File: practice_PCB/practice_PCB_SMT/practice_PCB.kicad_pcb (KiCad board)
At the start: 2 copper layers, 24.4 x 24.1 mm, 23 parts, among them J1 5V, J2 GND

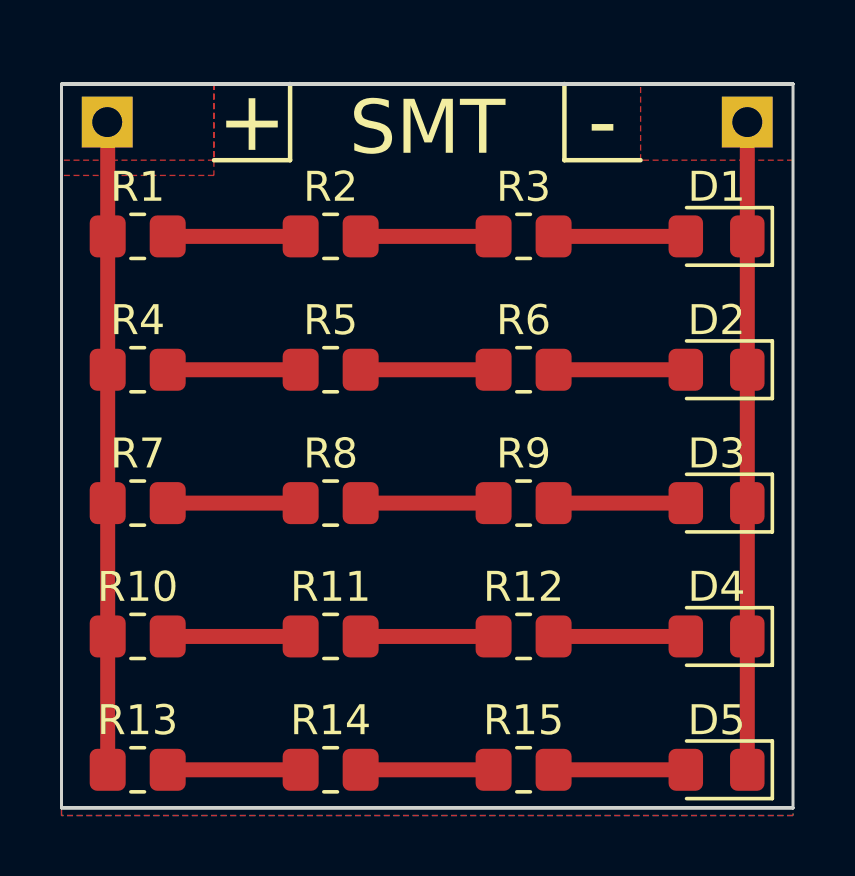
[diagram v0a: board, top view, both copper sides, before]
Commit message: fix some errors with the edge Cut Line
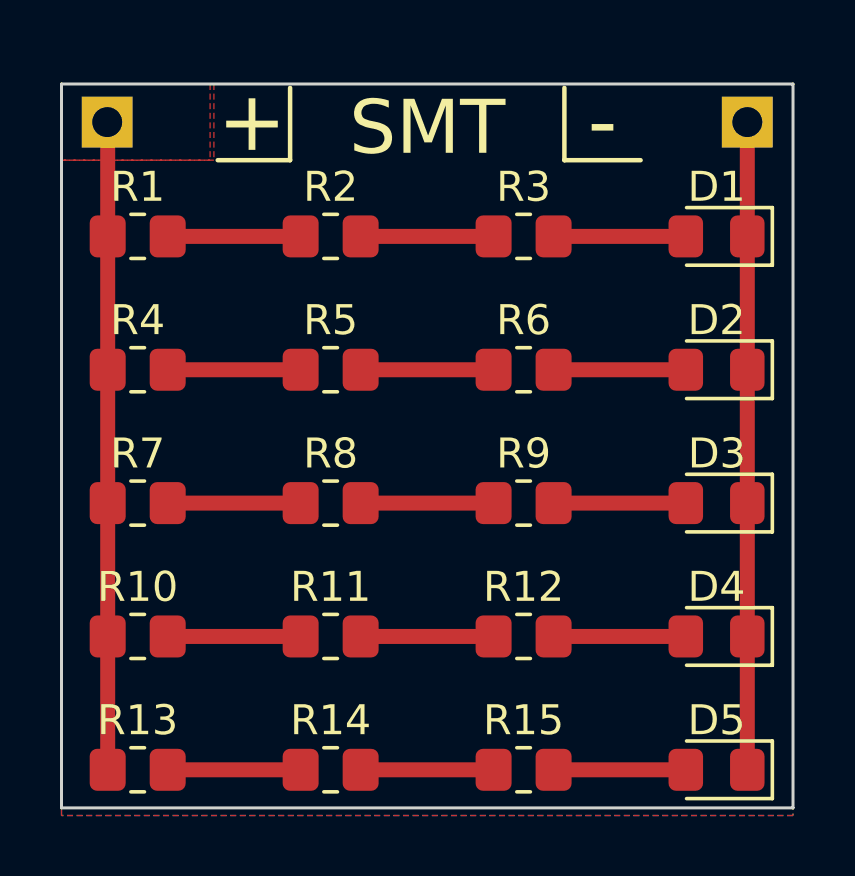
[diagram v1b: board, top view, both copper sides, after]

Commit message: make an array
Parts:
- added D10: LED, LED_SMD:LED_0805_2012Metric_Pad1.15x1.40mm_HandSolder, F.Cu at (183.4, 88.9)
- added D11: LED, LED_SMD:LED_0805_2012Metric_Pad1.15x1.40mm_HandSolder, F.Cu at (159.0, 95.2)
- added D12: LED, LED_SMD:LED_0805_2012Metric_Pad1.15x1.40mm_HandSolder, F.Cu at (159.0, 99.7)
- added D13: LED, LED_SMD:LED_0805_2012Metric_Pad1.15x1.40mm_HandSolder, F.Cu at (159.0, 104.1)
- added D14: LED, LED_SMD:LED_0805_2012Metric_Pad1.15x1.40mm_HandSolder, F.Cu at (159.0, 108.6)
- added D15: LED, LED_SMD:LED_0805_2012Metric_Pad1.15x1.40mm_HandSolder, F.Cu at (159.0, 113.0)
- added D16: LED, LED_SMD:LED_0805_2012Metric_Pad1.15x1.40mm_HandSolder, F.Cu at (183.4, 95.2)
- added D17: LED, LED_SMD:LED_0805_2012Metric_Pad1.15x1.40mm_HandSolder, F.Cu at (183.4, 99.7)
- added D18: LED, LED_SMD:LED_0805_2012Metric_Pad1.15x1.40mm_HandSolder, F.Cu at (183.4, 104.1)
- added D19: LED, LED_SMD:LED_0805_2012Metric_Pad1.15x1.40mm_HandSolder, F.Cu at (183.4, 108.6)
- added D20: LED, LED_SMD:LED_0805_2012Metric_Pad1.15x1.40mm_HandSolder, F.Cu at (183.4, 113.0)
- added D21: LED, LED_SMD:LED_0805_2012Metric_Pad1.15x1.40mm_HandSolder, F.Cu at (159.0, 119.4)
- added D22: LED, LED_SMD:LED_0805_2012Metric_Pad1.15x1.40mm_HandSolder, F.Cu at (159.0, 123.8)
- added D23: LED, LED_SMD:LED_0805_2012Metric_Pad1.15x1.40mm_HandSolder, F.Cu at (159.0, 128.3)
- added D24: LED, LED_SMD:LED_0805_2012Metric_Pad1.15x1.40mm_HandSolder, F.Cu at (159.0, 132.7)
- added D25: LED, LED_SMD:LED_0805_2012Metric_Pad1.15x1.40mm_HandSolder, F.Cu at (159.0, 137.2)
- added D26: LED, LED_SMD:LED_0805_2012Metric_Pad1.15x1.40mm_HandSolder, F.Cu at (183.4, 119.4)
- added D27: LED, LED_SMD:LED_0805_2012Metric_Pad1.15x1.40mm_HandSolder, F.Cu at (183.4, 123.8)
- added D28: LED, LED_SMD:LED_0805_2012Metric_Pad1.15x1.40mm_HandSolder, F.Cu at (183.4, 128.3)
- added D29: LED, LED_SMD:LED_0805_2012Metric_Pad1.15x1.40mm_HandSolder, F.Cu at (183.4, 132.7)
- added D30: LED, LED_SMD:LED_0805_2012Metric_Pad1.15x1.40mm_HandSolder, F.Cu at (183.4, 137.2)
- added D31: LED, LED_SMD:LED_0805_2012Metric_Pad1.15x1.40mm_HandSolder, F.Cu at (159.0, 143.5)
- added D32: LED, LED_SMD:LED_0805_2012Metric_Pad1.15x1.40mm_HandSolder, F.Cu at (159.0, 148.0)
- added D33: LED, LED_SMD:LED_0805_2012Metric_Pad1.15x1.40mm_HandSolder, F.Cu at (159.0, 152.4)
- added D34: LED, LED_SMD:LED_0805_2012Metric_Pad1.15x1.40mm_HandSolder, F.Cu at (159.0, 156.8)
- added D35: LED, LED_SMD:LED_0805_2012Metric_Pad1.15x1.40mm_HandSolder, F.Cu at (159.0, 161.3)
- added D36: LED, LED_SMD:LED_0805_2012Metric_Pad1.15x1.40mm_HandSolder, F.Cu at (183.4, 143.5)
- added D37: LED, LED_SMD:LED_0805_2012Metric_Pad1.15x1.40mm_HandSolder, F.Cu at (183.4, 148.0)
- added D38: LED, LED_SMD:LED_0805_2012Metric_Pad1.15x1.40mm_HandSolder, F.Cu at (183.4, 152.4)
- added D39: LED, LED_SMD:LED_0805_2012Metric_Pad1.15x1.40mm_HandSolder, F.Cu at (183.4, 156.8)
- added D40: LED, LED_SMD:LED_0805_2012Metric_Pad1.15x1.40mm_HandSolder, F.Cu at (183.4, 161.3)
- added D6: LED, LED_SMD:LED_0805_2012Metric_Pad1.15x1.40mm_HandSolder, F.Cu at (183.4, 71.1)
- added D7: LED, LED_SMD:LED_0805_2012Metric_Pad1.15x1.40mm_HandSolder, F.Cu at (183.4, 75.6)
- added D8: LED, LED_SMD:LED_0805_2012Metric_Pad1.15x1.40mm_HandSolder, F.Cu at (183.4, 80.0)
- added D9: LED, LED_SMD:LED_0805_2012Metric_Pad1.15x1.40mm_HandSolder, F.Cu at (183.4, 84.5)
- added G***1: LOGO, practice_PCB:MWG, B.Cu at (181.4, 86.4)
- added G***2: LOGO, practice_PCB:MWG, B.Cu at (157.0, 110.5)
- added G***3: LOGO, practice_PCB:MWG, B.Cu at (181.4, 110.5)
- added G***4: LOGO, practice_PCB:MWG, B.Cu at (157.0, 134.6)
- added G***5: LOGO, practice_PCB:MWG, B.Cu at (181.4, 134.6)
- added G***6: LOGO, practice_PCB:MWG, B.Cu at (157.0, 158.8)
- added G***7: LOGO, practice_PCB:MWG, B.Cu at (181.4, 158.8)
- added J10: GND, practice_PCB:PinSocket_1x01_P2.54mm_Vertical, F.Cu at (160.0, 115.6)
- added J11: 5V, practice_PCB:PinSocket_1x01_P2.54mm_Vertical, F.Cu at (163.1, 115.6)
- added J12: GND, practice_PCB:PinSocket_1x01_P2.54mm_Vertical, F.Cu at (184.4, 115.6)
- added J13: 5V, practice_PCB:PinSocket_1x01_P2.54mm_Vertical, F.Cu at (138.7, 139.7)
- added J14: GND, practice_PCB:PinSocket_1x01_P2.54mm_Vertical, F.Cu at (160.0, 139.7)
- added J15: 5V, practice_PCB:PinSocket_1x01_P2.54mm_Vertical, F.Cu at (163.1, 139.7)
- added J16: GND, practice_PCB:PinSocket_1x01_P2.54mm_Vertical, F.Cu at (184.4, 139.7)
- added J3: 5V, practice_PCB:PinSocket_1x01_P2.54mm_Vertical, F.Cu at (163.1, 67.3)
- added J4: GND, practice_PCB:PinSocket_1x01_P2.54mm_Vertical, F.Cu at (184.4, 67.3)
- added J5: 5V, practice_PCB:PinSocket_1x01_P2.54mm_Vertical, F.Cu at (138.7, 91.4)
- added J6: GND, practice_PCB:PinSocket_1x01_P2.54mm_Vertical, F.Cu at (160.0, 91.4)
- added J7: 5V, practice_PCB:PinSocket_1x01_P2.54mm_Vertical, F.Cu at (163.1, 91.4)
- added J8: GND, practice_PCB:PinSocket_1x01_P2.54mm_Vertical, F.Cu at (184.4, 91.4)
- added J9: 5V, practice_PCB:PinSocket_1x01_P2.54mm_Vertical, F.Cu at (138.7, 115.6)
- added R100: 60, Resistor_SMD:R_0805_2012Metric_Pad1.20x1.40mm_HandSolder, F.Cu at (139.7, 156.8)
- added R101: 60, Resistor_SMD:R_0805_2012Metric_Pad1.20x1.40mm_HandSolder, F.Cu at (146.1, 156.8)
- added R102: 60, Resistor_SMD:R_0805_2012Metric_Pad1.20x1.40mm_HandSolder, F.Cu at (152.6, 156.8)
- added R103: 60, Resistor_SMD:R_0805_2012Metric_Pad1.20x1.40mm_HandSolder, F.Cu at (139.7, 161.3)
- added R104: 60, Resistor_SMD:R_0805_2012Metric_Pad1.20x1.40mm_HandSolder, F.Cu at (146.1, 161.3)
- added R105: 60, Resistor_SMD:R_0805_2012Metric_Pad1.20x1.40mm_HandSolder, F.Cu at (152.6, 161.3)
- added R106: 60, Resistor_SMD:R_0805_2012Metric_Pad1.20x1.40mm_HandSolder, F.Cu at (164.1, 143.5)
- added R107: 60, Resistor_SMD:R_0805_2012Metric_Pad1.20x1.40mm_HandSolder, F.Cu at (170.5, 143.5)
- added R108: 60, Resistor_SMD:R_0805_2012Metric_Pad1.20x1.40mm_HandSolder, F.Cu at (176.9, 143.5)
- added R109: 60, Resistor_SMD:R_0805_2012Metric_Pad1.20x1.40mm_HandSolder, F.Cu at (164.1, 148.0)
- added R110: 60, Resistor_SMD:R_0805_2012Metric_Pad1.20x1.40mm_HandSolder, F.Cu at (170.5, 148.0)
- added R111: 60, Resistor_SMD:R_0805_2012Metric_Pad1.20x1.40mm_HandSolder, F.Cu at (176.9, 148.0)
- added R112: 60, Resistor_SMD:R_0805_2012Metric_Pad1.20x1.40mm_HandSolder, F.Cu at (164.1, 152.4)
- added R113: 60, Resistor_SMD:R_0805_2012Metric_Pad1.20x1.40mm_HandSolder, F.Cu at (170.5, 152.4)
- added R114: 60, Resistor_SMD:R_0805_2012Metric_Pad1.20x1.40mm_HandSolder, F.Cu at (176.9, 152.4)
- added R115: 60, Resistor_SMD:R_0805_2012Metric_Pad1.20x1.40mm_HandSolder, F.Cu at (164.1, 156.8)
- added R116: 60, Resistor_SMD:R_0805_2012Metric_Pad1.20x1.40mm_HandSolder, F.Cu at (170.5, 156.8)
- added R117: 60, Resistor_SMD:R_0805_2012Metric_Pad1.20x1.40mm_HandSolder, F.Cu at (176.9, 156.8)
- added R118: 60, Resistor_SMD:R_0805_2012Metric_Pad1.20x1.40mm_HandSolder, F.Cu at (164.1, 161.3)
- added R119: 60, Resistor_SMD:R_0805_2012Metric_Pad1.20x1.40mm_HandSolder, F.Cu at (170.5, 161.3)
- added R120: 60, Resistor_SMD:R_0805_2012Metric_Pad1.20x1.40mm_HandSolder, F.Cu at (176.9, 161.3)
- added R16: 60, Resistor_SMD:R_0805_2012Metric_Pad1.20x1.40mm_HandSolder, F.Cu at (164.1, 71.1)
- added R17: 60, Resistor_SMD:R_0805_2012Metric_Pad1.20x1.40mm_HandSolder, F.Cu at (170.5, 71.1)
- added R18: 60, Resistor_SMD:R_0805_2012Metric_Pad1.20x1.40mm_HandSolder, F.Cu at (176.9, 71.1)
- added R19: 60, Resistor_SMD:R_0805_2012Metric_Pad1.20x1.40mm_HandSolder, F.Cu at (164.1, 75.6)
- added R20: 60, Resistor_SMD:R_0805_2012Metric_Pad1.20x1.40mm_HandSolder, F.Cu at (170.5, 75.6)
- added R21: 60, Resistor_SMD:R_0805_2012Metric_Pad1.20x1.40mm_HandSolder, F.Cu at (176.9, 75.6)
- added R22: 60, Resistor_SMD:R_0805_2012Metric_Pad1.20x1.40mm_HandSolder, F.Cu at (164.1, 80.0)
- added R23: 60, Resistor_SMD:R_0805_2012Metric_Pad1.20x1.40mm_HandSolder, F.Cu at (170.5, 80.0)
- added R24: 60, Resistor_SMD:R_0805_2012Metric_Pad1.20x1.40mm_HandSolder, F.Cu at (176.9, 80.0)
- added R25: 60, Resistor_SMD:R_0805_2012Metric_Pad1.20x1.40mm_HandSolder, F.Cu at (164.1, 84.5)
- added R26: 60, Resistor_SMD:R_0805_2012Metric_Pad1.20x1.40mm_HandSolder, F.Cu at (170.5, 84.5)
- added R27: 60, Resistor_SMD:R_0805_2012Metric_Pad1.20x1.40mm_HandSolder, F.Cu at (176.9, 84.5)
- added R28: 60, Resistor_SMD:R_0805_2012Metric_Pad1.20x1.40mm_HandSolder, F.Cu at (164.1, 88.9)
- added R29: 60, Resistor_SMD:R_0805_2012Metric_Pad1.20x1.40mm_HandSolder, F.Cu at (170.5, 88.9)
- added R30: 60, Resistor_SMD:R_0805_2012Metric_Pad1.20x1.40mm_HandSolder, F.Cu at (176.9, 88.9)
- added R31: 60, Resistor_SMD:R_0805_2012Metric_Pad1.20x1.40mm_HandSolder, F.Cu at (139.7, 95.2)
- added R32: 60, Resistor_SMD:R_0805_2012Metric_Pad1.20x1.40mm_HandSolder, F.Cu at (146.1, 95.2)
- added R33: 60, Resistor_SMD:R_0805_2012Metric_Pad1.20x1.40mm_HandSolder, F.Cu at (152.6, 95.2)
- added R34: 60, Resistor_SMD:R_0805_2012Metric_Pad1.20x1.40mm_HandSolder, F.Cu at (139.7, 99.7)
- added R35: 60, Resistor_SMD:R_0805_2012Metric_Pad1.20x1.40mm_HandSolder, F.Cu at (146.1, 99.7)
- added R36: 60, Resistor_SMD:R_0805_2012Metric_Pad1.20x1.40mm_HandSolder, F.Cu at (152.6, 99.7)
- added R37: 60, Resistor_SMD:R_0805_2012Metric_Pad1.20x1.40mm_HandSolder, F.Cu at (139.7, 104.1)
- added R38: 60, Resistor_SMD:R_0805_2012Metric_Pad1.20x1.40mm_HandSolder, F.Cu at (146.1, 104.1)
- added R39: 60, Resistor_SMD:R_0805_2012Metric_Pad1.20x1.40mm_HandSolder, F.Cu at (152.6, 104.1)
- added R40: 60, Resistor_SMD:R_0805_2012Metric_Pad1.20x1.40mm_HandSolder, F.Cu at (139.7, 108.6)
- added R41: 60, Resistor_SMD:R_0805_2012Metric_Pad1.20x1.40mm_HandSolder, F.Cu at (146.1, 108.6)
- added R42: 60, Resistor_SMD:R_0805_2012Metric_Pad1.20x1.40mm_HandSolder, F.Cu at (152.6, 108.6)
- added R43: 60, Resistor_SMD:R_0805_2012Metric_Pad1.20x1.40mm_HandSolder, F.Cu at (139.7, 113.0)
- added R44: 60, Resistor_SMD:R_0805_2012Metric_Pad1.20x1.40mm_HandSolder, F.Cu at (146.1, 113.0)
- added R45: 60, Resistor_SMD:R_0805_2012Metric_Pad1.20x1.40mm_HandSolder, F.Cu at (152.6, 113.0)
- added R46: 60, Resistor_SMD:R_0805_2012Metric_Pad1.20x1.40mm_HandSolder, F.Cu at (164.1, 95.2)
- added R47: 60, Resistor_SMD:R_0805_2012Metric_Pad1.20x1.40mm_HandSolder, F.Cu at (170.5, 95.2)
- added R48: 60, Resistor_SMD:R_0805_2012Metric_Pad1.20x1.40mm_HandSolder, F.Cu at (176.9, 95.2)
- added R49: 60, Resistor_SMD:R_0805_2012Metric_Pad1.20x1.40mm_HandSolder, F.Cu at (164.1, 99.7)
- added R50: 60, Resistor_SMD:R_0805_2012Metric_Pad1.20x1.40mm_HandSolder, F.Cu at (170.5, 99.7)
- added R51: 60, Resistor_SMD:R_0805_2012Metric_Pad1.20x1.40mm_HandSolder, F.Cu at (176.9, 99.7)
- added R52: 60, Resistor_SMD:R_0805_2012Metric_Pad1.20x1.40mm_HandSolder, F.Cu at (164.1, 104.1)
- added R53: 60, Resistor_SMD:R_0805_2012Metric_Pad1.20x1.40mm_HandSolder, F.Cu at (170.5, 104.1)
- added R54: 60, Resistor_SMD:R_0805_2012Metric_Pad1.20x1.40mm_HandSolder, F.Cu at (176.9, 104.1)
- added R55: 60, Resistor_SMD:R_0805_2012Metric_Pad1.20x1.40mm_HandSolder, F.Cu at (164.1, 108.6)
- added R56: 60, Resistor_SMD:R_0805_2012Metric_Pad1.20x1.40mm_HandSolder, F.Cu at (170.5, 108.6)
- added R57: 60, Resistor_SMD:R_0805_2012Metric_Pad1.20x1.40mm_HandSolder, F.Cu at (176.9, 108.6)
- added R58: 60, Resistor_SMD:R_0805_2012Metric_Pad1.20x1.40mm_HandSolder, F.Cu at (164.1, 113.0)
- added R59: 60, Resistor_SMD:R_0805_2012Metric_Pad1.20x1.40mm_HandSolder, F.Cu at (170.5, 113.0)
- added R60: 60, Resistor_SMD:R_0805_2012Metric_Pad1.20x1.40mm_HandSolder, F.Cu at (176.9, 113.0)
- added R61: 60, Resistor_SMD:R_0805_2012Metric_Pad1.20x1.40mm_HandSolder, F.Cu at (139.7, 119.4)
- added R62: 60, Resistor_SMD:R_0805_2012Metric_Pad1.20x1.40mm_HandSolder, F.Cu at (146.1, 119.4)
- added R63: 60, Resistor_SMD:R_0805_2012Metric_Pad1.20x1.40mm_HandSolder, F.Cu at (152.6, 119.4)
- added R64: 60, Resistor_SMD:R_0805_2012Metric_Pad1.20x1.40mm_HandSolder, F.Cu at (139.7, 123.8)
- added R65: 60, Resistor_SMD:R_0805_2012Metric_Pad1.20x1.40mm_HandSolder, F.Cu at (146.1, 123.8)
- added R66: 60, Resistor_SMD:R_0805_2012Metric_Pad1.20x1.40mm_HandSolder, F.Cu at (152.6, 123.8)
- added R67: 60, Resistor_SMD:R_0805_2012Metric_Pad1.20x1.40mm_HandSolder, F.Cu at (139.7, 128.3)
- added R68: 60, Resistor_SMD:R_0805_2012Metric_Pad1.20x1.40mm_HandSolder, F.Cu at (146.1, 128.3)
- added R69: 60, Resistor_SMD:R_0805_2012Metric_Pad1.20x1.40mm_HandSolder, F.Cu at (152.6, 128.3)
- added R70: 60, Resistor_SMD:R_0805_2012Metric_Pad1.20x1.40mm_HandSolder, F.Cu at (139.7, 132.7)
- added R71: 60, Resistor_SMD:R_0805_2012Metric_Pad1.20x1.40mm_HandSolder, F.Cu at (146.1, 132.7)
- added R72: 60, Resistor_SMD:R_0805_2012Metric_Pad1.20x1.40mm_HandSolder, F.Cu at (152.6, 132.7)
- added R73: 60, Resistor_SMD:R_0805_2012Metric_Pad1.20x1.40mm_HandSolder, F.Cu at (139.7, 137.2)
- added R74: 60, Resistor_SMD:R_0805_2012Metric_Pad1.20x1.40mm_HandSolder, F.Cu at (146.1, 137.2)
- added R75: 60, Resistor_SMD:R_0805_2012Metric_Pad1.20x1.40mm_HandSolder, F.Cu at (152.6, 137.2)
- added R76: 60, Resistor_SMD:R_0805_2012Metric_Pad1.20x1.40mm_HandSolder, F.Cu at (164.1, 119.4)
- added R77: 60, Resistor_SMD:R_0805_2012Metric_Pad1.20x1.40mm_HandSolder, F.Cu at (170.5, 119.4)
- added R78: 60, Resistor_SMD:R_0805_2012Metric_Pad1.20x1.40mm_HandSolder, F.Cu at (176.9, 119.4)
- added R79: 60, Resistor_SMD:R_0805_2012Metric_Pad1.20x1.40mm_HandSolder, F.Cu at (164.1, 123.8)
- added R80: 60, Resistor_SMD:R_0805_2012Metric_Pad1.20x1.40mm_HandSolder, F.Cu at (170.5, 123.8)
- added R81: 60, Resistor_SMD:R_0805_2012Metric_Pad1.20x1.40mm_HandSolder, F.Cu at (176.9, 123.8)
- added R82: 60, Resistor_SMD:R_0805_2012Metric_Pad1.20x1.40mm_HandSolder, F.Cu at (164.1, 128.3)
- added R83: 60, Resistor_SMD:R_0805_2012Metric_Pad1.20x1.40mm_HandSolder, F.Cu at (170.5, 128.3)
- added R84: 60, Resistor_SMD:R_0805_2012Metric_Pad1.20x1.40mm_HandSolder, F.Cu at (176.9, 128.3)
- added R85: 60, Resistor_SMD:R_0805_2012Metric_Pad1.20x1.40mm_HandSolder, F.Cu at (164.1, 132.7)
- added R86: 60, Resistor_SMD:R_0805_2012Metric_Pad1.20x1.40mm_HandSolder, F.Cu at (170.5, 132.7)
- added R87: 60, Resistor_SMD:R_0805_2012Metric_Pad1.20x1.40mm_HandSolder, F.Cu at (176.9, 132.7)
- added R88: 60, Resistor_SMD:R_0805_2012Metric_Pad1.20x1.40mm_HandSolder, F.Cu at (164.1, 137.2)
- added R89: 60, Resistor_SMD:R_0805_2012Metric_Pad1.20x1.40mm_HandSolder, F.Cu at (170.5, 137.2)
- added R90: 60, Resistor_SMD:R_0805_2012Metric_Pad1.20x1.40mm_HandSolder, F.Cu at (176.9, 137.2)
- added R91: 60, Resistor_SMD:R_0805_2012Metric_Pad1.20x1.40mm_HandSolder, F.Cu at (139.7, 143.5)
- added R92: 60, Resistor_SMD:R_0805_2012Metric_Pad1.20x1.40mm_HandSolder, F.Cu at (146.1, 143.5)
- added R93: 60, Resistor_SMD:R_0805_2012Metric_Pad1.20x1.40mm_HandSolder, F.Cu at (152.6, 143.5)
- added R94: 60, Resistor_SMD:R_0805_2012Metric_Pad1.20x1.40mm_HandSolder, F.Cu at (139.7, 148.0)
- added R95: 60, Resistor_SMD:R_0805_2012Metric_Pad1.20x1.40mm_HandSolder, F.Cu at (146.1, 148.0)
- added R96: 60, Resistor_SMD:R_0805_2012Metric_Pad1.20x1.40mm_HandSolder, F.Cu at (152.6, 148.0)
- added R97: 60, Resistor_SMD:R_0805_2012Metric_Pad1.20x1.40mm_HandSolder, F.Cu at (139.7, 152.4)
- added R98: 60, Resistor_SMD:R_0805_2012Metric_Pad1.20x1.40mm_HandSolder, F.Cu at (146.1, 152.4)
- added R99: 60, Resistor_SMD:R_0805_2012Metric_Pad1.20x1.40mm_HandSolder, F.Cu at (152.6, 152.4)
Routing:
- net +5V: track 21.6 -> 172.8 mm
- net GND: track 21.6 -> 172.7 mm
- net Net-(R7-Pad2): track 4.43 -> 35.5 mm
- net Net-(R4-Pad2): track 4.43 -> 35.5 mm
- net Net-(R13-Pad2): track 4.43 -> 35.5 mm
- net Net-(R10-Pad2): track 4.43 -> 35.5 mm
- net Net-(R1-Pad2): track 4.43 -> 35.5 mm
- net Net-(R8-Pad2): track 4.43 -> 35.5 mm
- net Net-(R5-Pad2): track 4.43 -> 35.5 mm
- net Net-(R2-Pad2): track 4.43 -> 35.5 mm
- net Net-(R14-Pad2): track 4.43 -> 35.5 mm
- net Net-(R11-Pad2): track 4.43 -> 35.5 mm
- net Net-(D5-Pad2): track 4.41 -> 35.3 mm
- net Net-(D4-Pad2): track 4.41 -> 35.3 mm
- net Net-(D3-Pad2): track 4.41 -> 35.3 mm
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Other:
- board size 24.4 x 24.1 mm -> 48.8 x 96.5 mm
